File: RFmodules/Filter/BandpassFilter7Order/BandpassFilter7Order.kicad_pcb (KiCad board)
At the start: 2 copper layers, 31.2 x 7.1 mm, 17 parts, among them J1 SMA, J2 SMA

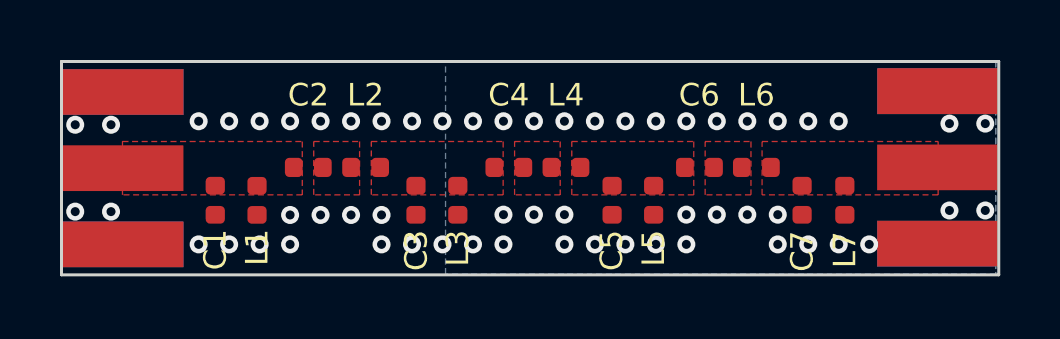
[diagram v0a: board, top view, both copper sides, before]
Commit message: Fix design guide issues and typos
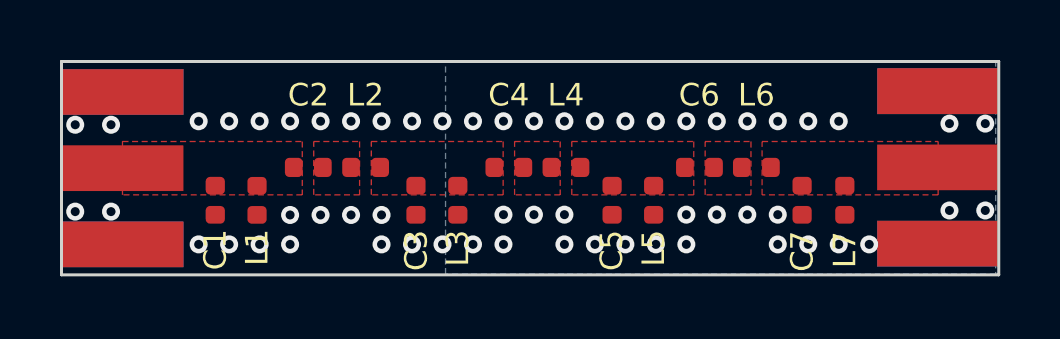
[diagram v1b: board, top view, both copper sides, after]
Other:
- board text added: "Bandpass Filter 7th Order Revision 0.1.0 - 01/2019 github.com/fgaletsee/RFLego"
- board text removed: "Bandpass Filter 7 Order Revision 0.1.0 - 01/2019 github.com/fgaletsee/RFLego"
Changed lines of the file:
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@@
   (page A4)
   (layers
-    (0 F.Cu signal hide)
-    (31 B.Cu signal hide)
+    (0 F.Cu signal)
+    (31 B.Cu signal)
     (32 B.Adhes user)
     (33 F.Adhes user)
@@
   (gr_line (start 168.402 104.394) (end 137.16 104.394) (layer Edge.Cuts) (width 0.1))
   (gr_line (start 162.8394 110.0582) (end 150.5458 110.0582) (layer B.SilkS) (width 2.5))
-  (gr_text "Bandpass Filter 7 Order\nRevision 0.1.0 - 01/2019\ngithub.com/fgaletsee/RFLego" (at 164.2364 106.6038) (layer B.SilkS)
+  (gr_text "Bandpass Filter 7th Order\nRevision 0.1.0 - 01/2019\ngithub.com/fgaletsee/RFLego" (at 164.2364 106.6038) (layer B.SilkS)
     (effects (font (size 0.75 0.75) (thickness 0.1875)) (justify left mirror))
   )
@@
       )
     )
-  )
-  (zone (net 2) (net_name GND) (layer B.Cu) (hatch edge 0.508)
-    (connect_pads yes (clearance 0.1))
-    (min_thickness 0.1)
-    (fill yes (arc_segments 16) (thermal_gap 0.508) (thermal_bridge_width 0.508))
-    (polygon
-      (pts
-        (xy 137.16 104.394) (xy 168.3004 104.394) (xy 168.3004 111.506) (xy 137.16 111.506)
-      )
-    )

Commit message: Update board descriptions, add Bandstop elliptic filter 5th order
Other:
- board text added: "Bandpass Filter 7th Order Revision 1 - 01/2019 github.com/fgaletsee/RFLego"
- board text removed: "Bandpass Filter 7th Order Revision 0.1.0 - 01/2019 github.com/fgaletsee/RFLego"
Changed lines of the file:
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@@
   (gr_line (start 168.402 104.394) (end 137.16 104.394) (layer Edge.Cuts) (width 0.1))
   (gr_line (start 162.8394 110.0582) (end 150.5458 110.0582) (layer B.SilkS) (width 2.5))
-  (gr_text "Bandpass Filter 7th Order\nRevision 0.1.0 - 01/2019\ngithub.com/fgaletsee/RFLego" (at 164.2364 106.6038) (layer B.SilkS)
+  (gr_text "Bandpass Filter 7th Order\nRevision 1 - 01/2019\ngithub.com/fgaletsee/RFLego" (at 164.2364 106.6038) (layer B.SilkS)
     (effects (font (size 0.75 0.75) (thickness 0.1875)) (justify left mirror))
   )
